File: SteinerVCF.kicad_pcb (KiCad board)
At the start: 2 copper layers, 39.6 x 100 mm, 72 parts, among them J1 AudioJack2_Ground_Switch, J2 AudioJack2_Ground_Switch, J3 AudioJack2_Ground_Switch, J4 AudioJack2_Ground_Switch, J5 AudioJack2_Ground_Switch, J6 AudioJack2_Ground_Switch, J7 Conn_02x05_Odd_Even, J8 AudioJack2_Ground_Switch, J9 AudioJack2_Ground_Switch, Q1 BC847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

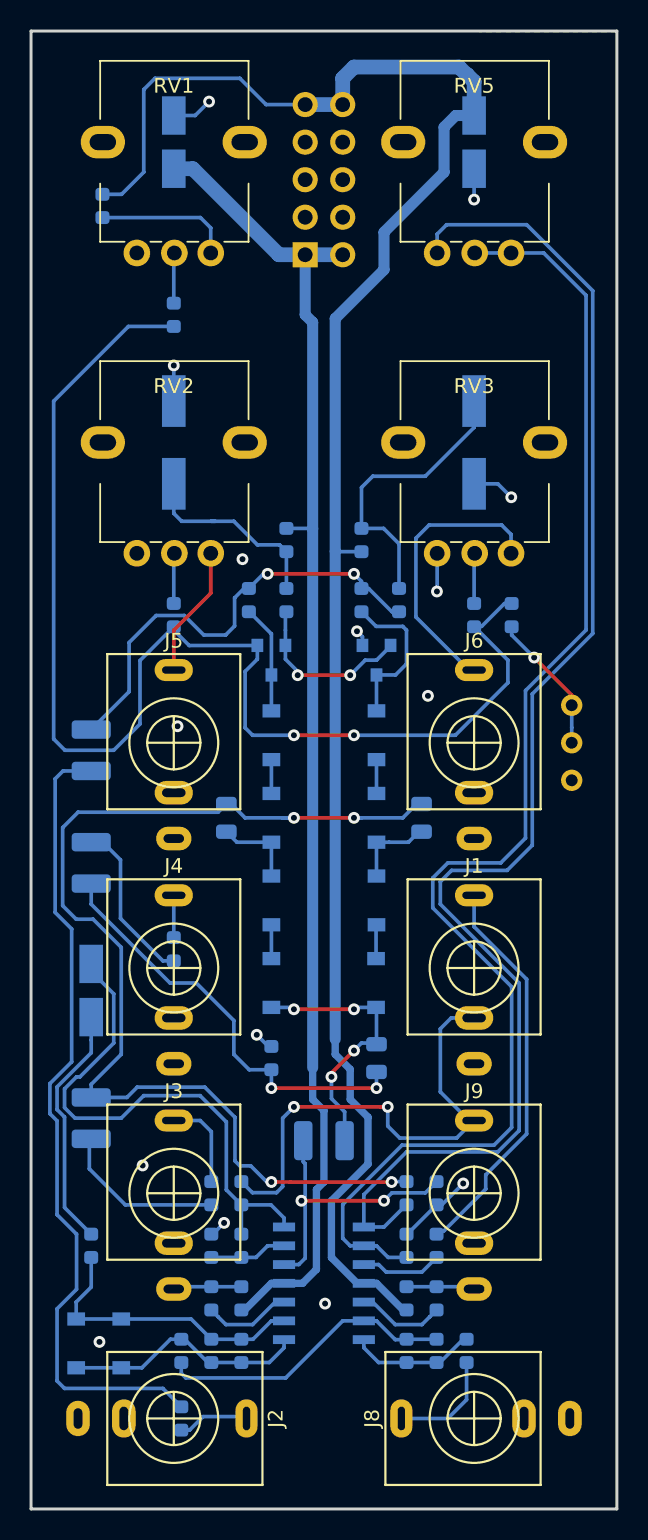
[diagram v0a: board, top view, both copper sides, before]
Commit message: Better placement of large caps.
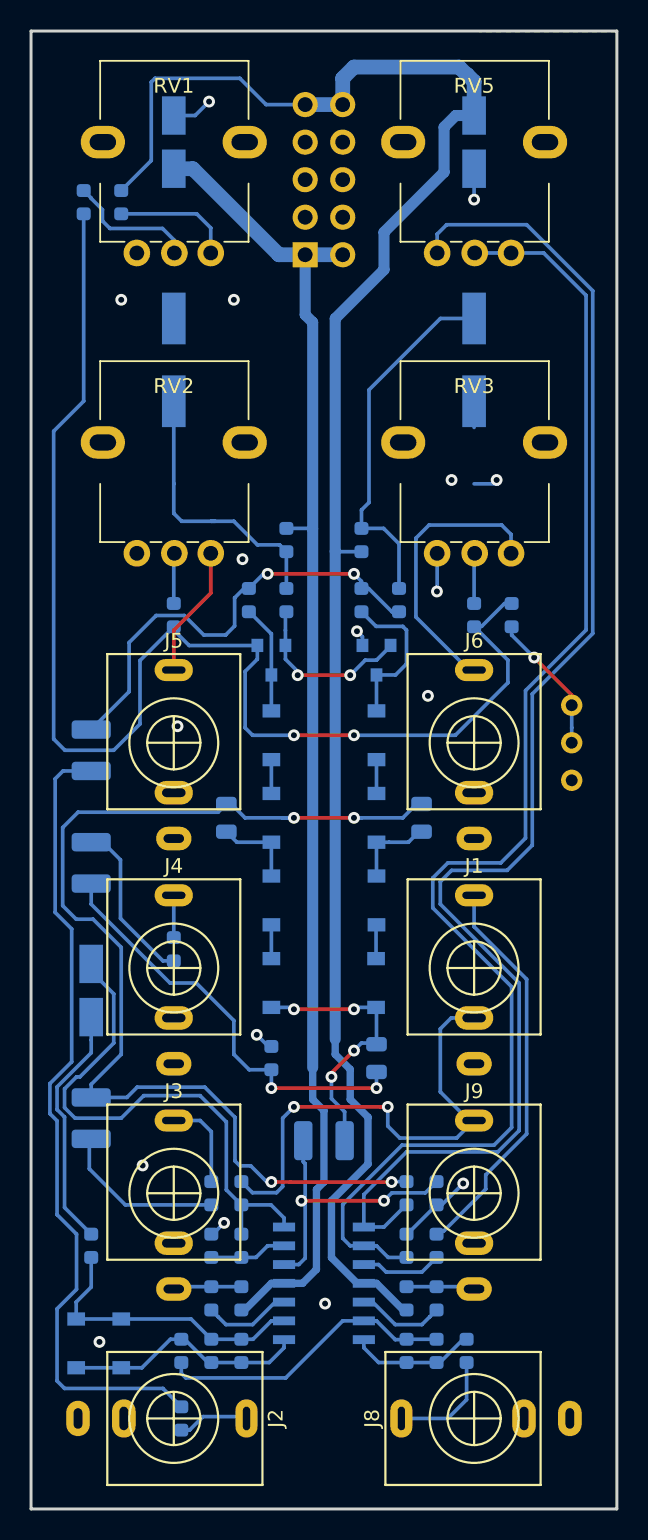
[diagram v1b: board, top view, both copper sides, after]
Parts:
- moved R4 9.76 mm to (132.2, 68.4)
- moved C6 5.59 mm to (138.3, 79.1)
- moved C7 5.59 mm to (158.7, 79.1)
- moved R1 1.30 mm to (134.8, 68.4)
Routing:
- net Net-(C6-Pad2): track 13.5 -> 19.1 mm
- net /CutOff: track 3.41 -> 8.90 mm
- net Net-(C7-Pad1): track 19.8 -> 24.7 mm
- net Net-(Q1-Pad1): track 87.1 -> 90.4 mm
- net GND: track 30.9 -> 29.3 mm, vias 15 -> 17
- net +12V: track 129.4 -> 127.8 mm
- net Net-(R1-Pad1): track 9.37 -> 8.20 mm
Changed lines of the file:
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@@
     (thickness 1.6)
     (drawings 58)
-    (tracks 499)
+    (tracks 508)
     (zones 0)
     (modules 72)
@@
   )
   (module Capacitor_SMD:CP_Elec_6.3x5.4 (layer B.Cu)
-    (at 138.34 84.68 270)
+    (at 138.34 79.092 270)
     (descr "SMT capacitor, aluminium electrolytic, 6.3x5.4, Panasonic C55 ")
     (tags "Capacitor Electrolytic")
@@
   )
   (module Capacitor_SMD:CP_Elec_6.3x5.4 (layer B.Cu)
-    (at 158.66 84.68 270)
+    (at 158.66 79.092 270)
     (descr "SMT capacitor, aluminium electrolytic, 6.3x5.4, Panasonic C55 ")
     (tags "Capacitor Electrolytic")
@@
   )
   (module Resistor_SMD:R_0603_1608Metric (layer B.Cu)
-    (at 138.34 76.044 90)
+    (at 132.244 68.424 90)
     (descr "Resistor SMD 0603 (1608 Metric), square (rectangular) end terminal, IPC_7351 nominal, (Body size source: http://www.tortai-tech.com/upload/download/2011102023233369053.pdf), generated with kicad-footprint-generator")
     (tags resistor)
@@
   )
   (module Resistor_SMD:R_0603_1608Metric (layer B.Cu)
-    (at 133.514 68.678 90)
+    (at 134.784 68.424 90)
     (descr "Resistor SMD 0603 (1608 Metric), square (rectangular) end terminal, IPC_7351 nominal, (Body size source: http://www.tortai-tech.com/upload/download/2011102023233369053.pdf), generated with kicad-footprint-generator")
     (tags resistor)
@@
   (segment (start 150.75 141.576) (end 149.008 139.834) (width 0.5) (layer B.Cu) (net 20))
   (segment (start 151.2 141.576) (end 150.75 141.576) (width 0.5) (layer B.Cu) (net 20))
-  (segment (start 136.308 66.392) (end 134.8095 67.8905) (width 0.25) (layer B.Cu) (net 20))
-  (segment (start 136.308 60.804) (end 136.308 66.392) (width 0.25) (layer B.Cu) (net 20))
-  (segment (start 137.07 60.042) (end 136.308 60.804) (width 0.25) (layer B.Cu) (net 20))
-  (segment (start 134.8095 67.8905) (end 133.514 67.8905) (width 0.25) (layer B.Cu) (net 20))
-  (segment (start 144.5884 61.82) (end 142.8104 60.042) (width 0.25) (layer B.Cu) (net 20))
+  (segment (start 136.816 60.296) (end 136.816 65.6045) (width 0.25) (layer B.Cu) (net 20))
   (segment (start 142.8104 60.042) (end 137.07 60.042) (width 0.25) (layer B.Cu) (net 20))
+  (segment (start 136.816 65.6045) (end 134.784 67.6365) (width 0.25) (layer B.Cu) (net 20))
+  (segment (start 144.5884 61.82) (end 142.8104 60.042) (width 0.25) (layer B.Cu) (net 20))
+  (segment (start 137.07 60.042) (end 136.816 60.296) (width 0.25) (layer B.Cu) (net 20))
   (segment (start 147.23 61.82) (end 144.5884 61.82) (width 0.25) (layer B.Cu) (net 20))
   (segment (start 140.88 71.90001) (end 140.84 71.86001) (width 0.25) (layer B.Cu) (net 21))
-  (segment (start 140.84 70.162) (end 140.84 71.86001) (width 0.25) (layer B.Cu) (net 21))
-  (segment (start 140.1435 69.4655) (end 140.84 70.162) (width 0.25) (layer B.Cu) (net 21))
-  (segment (start 133.514 69.4655) (end 140.1435 69.4655) (width 0.25) (layer B.Cu) (net 21))
+  (segment (start 140.84 70.162) (end 139.8895 69.2115) (width 0.25) (layer B.Cu) (net 21))
+  (segment (start 139.8895 69.2115) (end 134.784 69.2115) (width 0.25) (layer B.Cu) (net 21))
+  (segment (start 140.84 71.86001) (end 140.84 70.162) (width 0.25) (layer B.Cu) (net 21))
   (segment (start 138.346 87.48) (end 138.34 87.48) (width 0.25) (layer B.Cu) (net 22))
   (segment (start 145.96 94.5605) (end 145.9345 94.5605) (width 0.25) (layer B.Cu) (net 22))
@@
   (segment (start 153.58 91.538) (end 152.5385 90.4965) (width 0.25) (layer B.Cu) (net 26))
   (segment (start 153.58 94.5605) (end 153.58 91.538) (width 0.25) (layer B.Cu) (net 26))
-  (segment (start 151.04 87.728) (end 151.04 90.4965) (width 0.25) (layer B.Cu) (net 26))
-  (segment (start 151.802 86.966) (end 151.04 87.728) (width 0.25) (layer B.Cu) (net 26))
-  (segment (start 158.66 83.664) (end 155.358 86.966) (width 0.25) (layer B.Cu) (net 26))
-  (segment (start 155.358 86.966) (end 151.802 86.966) (width 0.25) (layer B.Cu) (net 26))
-  (segment (start 158.66 81.88) (end 158.66 83.664) (width 0.25) (layer B.Cu) (net 26))
+  (segment (start 156.38 76.292) (end 158.66 76.292) (width 0.25) (layer B.Cu) (net 26))
+  (segment (start 151.548 81.124) (end 156.38 76.292) (width 0.25) (layer B.Cu) (net 26))
+  (segment (start 151.548 88.744) (end 151.548 81.124) (width 0.25) (layer B.Cu) (net 26))
+  (segment (start 151.04 89.252) (end 151.548 88.744) (width 0.25) (layer B.Cu) (net 26))
+  (segment (start 151.04 90.4965) (end 151.04 89.252) (width 0.25) (layer B.Cu) (net 26))
+  (segment (start 158.66 81.88) (end 158.66 83.664) (width 0.25) (layer B.Cu) (net 55))
   (segment (start 165.264 103.981767) (end 165.264 102.46) (width 0.25) (layer B.Cu) (net 27))
   (segment (start 165.264 105) (end 165.264 103.981767) (width 0.25) (layer B.Cu) (net 27))
@@
   (segment (start 134.276 105.508) (end 136.054 103.73) (width 0.25) (layer B.Cu) (net 28))
   (segment (start 130.212 104.746) (end 130.974 105.508) (width 0.25) (layer B.Cu) (net 28))
-  (segment (start 130.212 81.886) (end 130.212 104.746) (width 0.25) (layer B.Cu) (net 28))
-  (segment (start 135.2665 76.8315) (end 130.212 81.886) (width 0.25) (layer B.Cu) (net 28))
   (segment (start 130.974 105.508) (end 134.276 105.508) (width 0.25) (layer B.Cu) (net 28))
   (segment (start 136.054 99.4375) (end 138.34 97.1515) (width 0.25) (layer B.Cu) (net 28))
-  (segment (start 138.34 76.8315) (end 135.2665 76.8315) (width 0.25) (layer B.Cu) (net 28))
   (segment (start 139.3814 98.4214) (end 138.34 97.38) (width 0.25) (layer B.Cu) (net 28))
   (segment (start 138.34 97.38) (end 138.34 97.1515) (width 0.25) (layer B.Cu) (net 28))
   (segment (start 143.9846 98.4214) (end 139.3814 98.4214) (width 0.25) (layer B.Cu) (net 28))
   (segment (start 143.994 98.412) (end 143.9846 98.4214) (width 0.25) (layer B.Cu) (net 28))
+  (segment (start 132.244 81.886) (end 130.212 83.918) (width 0.25) (layer B.Cu) (net 28))
+  (segment (start 130.212 83.918) (end 130.212 104.746) (width 0.25) (layer B.Cu) (net 28))
+  (segment (start 132.244 69.2115) (end 132.244 81.886) (width 0.25) (layer B.Cu) (net 28))
   (segment (start 144.944 102.842) (end 144.944 100.412) (width 0.25) (layer B.Cu) (net 29))
   (segment (start 144.944 97.634) (end 143.4455 96.1355) (width 0.25) (layer B.Cu) (net 29))
@@
   (segment (start 130.844 106.908) (end 130.3136 107.4384) (width 0.25) (layer B.Cu) (net 35))
   (segment (start 138.34 71.90001) (end 138.38 71.86001) (width 0.25) (layer B.Cu) (net 36))
-  (segment (start 138.34 75.2565) (end 138.34 71.90001) (width 0.25) (layer B.Cu) (net 36))
+  (segment (start 132.752 68.1445) (end 132.244 67.6365) (width 0.25) (layer B.Cu) (net 36))
+  (segment (start 133.514 68.932) (end 132.752 68.17) (width 0.25) (layer B.Cu) (net 36))
+  (segment (start 133.514 69.694) (end 133.514 68.932) (width 0.25) (layer B.Cu) (net 36))
+  (segment (start 132.752 68.17) (end 132.752 68.1445) (width 0.25) (layer B.Cu) (net 36))
+  (segment (start 138.38 71.86001) (end 138.38 71.004) (width 0.25) (layer B.Cu) (net 36))
+  (segment (start 134.022 70.202) (end 133.514 69.694) (width 0.25) (layer B.Cu) (net 36))
+  (segment (start 137.578 70.202) (end 134.022 70.202) (width 0.25) (layer B.Cu) (net 36))
+  (segment (start 138.38 71.004) (end 137.578 70.202) (width 0.25) (layer B.Cu) (net 36))
   (segment (start 158.66 92.22001) (end 158.7 92.18001) (width 0.25) (layer B.Cu) (net 37))
   (segment (start 158.66 95.5765) (end 158.66 92.22001) (width 0.25) (layer B.Cu) (net 37))
@@
   (segment (start 141.896 111.0175) (end 142.6085 111.73) (width 0.25) (layer B.Cu) (net 53))
   (segment (start 144.944 108.43) (end 144.944 106.142) (width 0.25) (layer B.Cu) (net 54))
-  (via (at 138.34 79.473) (size 0.8) (drill 0.4) (layers F.Cu B.Cu) (net 55))
-  (segment (start 138.34 81.88) (end 138.34 79.473) (width 0.25) (layer B.Cu) (net 55))
+  (segment (start 138.34 87.48) (end 138.34 81.892) (width 0.25) (layer B.Cu) (net 22))
   (via (at 158.66 68.2462) (size 0.8) (drill 0.4) (layers F.Cu B.Cu) (net 55))
   (segment (start 158.66 66.16) (end 158.66 68.2462) (width 0.25) (layer B.Cu) (net 55))
@@
   (segment (start 139.7844 62.56) (end 140.7276 61.6168) (width 0.25) (layer B.Cu) (net 55))
   (segment (start 138.34 62.56) (end 139.7844 62.56) (width 0.25) (layer B.Cu) (net 55))
-  (via (at 161.1746 88.3884) (size 0.8) (drill 0.4) (layers F.Cu B.Cu) (net 55))
-  (segment (start 160.2662 87.48) (end 161.1746 88.3884) (width 0.25) (layer B.Cu) (net 55))
-  (segment (start 158.66 87.48) (end 160.2662 87.48) (width 0.25) (layer B.Cu) (net 55))
   (via (at 156.1454 94.7638) (size 0.8) (drill 0.4) (layers F.Cu B.Cu) (net 55))
   (segment (start 156.16 94.7492) (end 156.1454 94.7638) (width 0.25) (layer B.Cu) (net 55))
@@
   (segment (start 140.88 138.2485) (end 140.9817 138.2485) (width 0.25) (layer B.Cu) (net 55))
   (via (at 142.9882 92.5794) (size 0.8) (drill 0.4) (layers F.Cu B.Cu) (net 55))
+  (segment (start 160.2662 87.48) (end 158.66 87.48) (width 0.25) (layer B.Cu) (net 55))
+  (segment (start 160.184 87.22) (end 160.2662 87.48) (width 0.25) (layer B.Cu) (net 55))
+  (via (at 160.184 87.22) (size 0.8) (drill 0.4) (layers F.Cu B.Cu) (net 55))
+  (via (at 157.136 87.22) (size 0.8) (drill 0.4) (layers F.Cu B.Cu) (net 55))
+  (via (at 142.404 75.028) (size 0.8) (drill 0.4) (layers F.Cu B.Cu) (net 55))
+  (via (at 134.784 75.028) (size 0.8) (drill 0.4) (layers F.Cu B.Cu) (net 55))
   (zone (net 55) (net_name GND) (layer F.Cu) (hatch edge 0.508)
     (connect_pads (clearance 0.508))

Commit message: Moved some caps away from the edge.
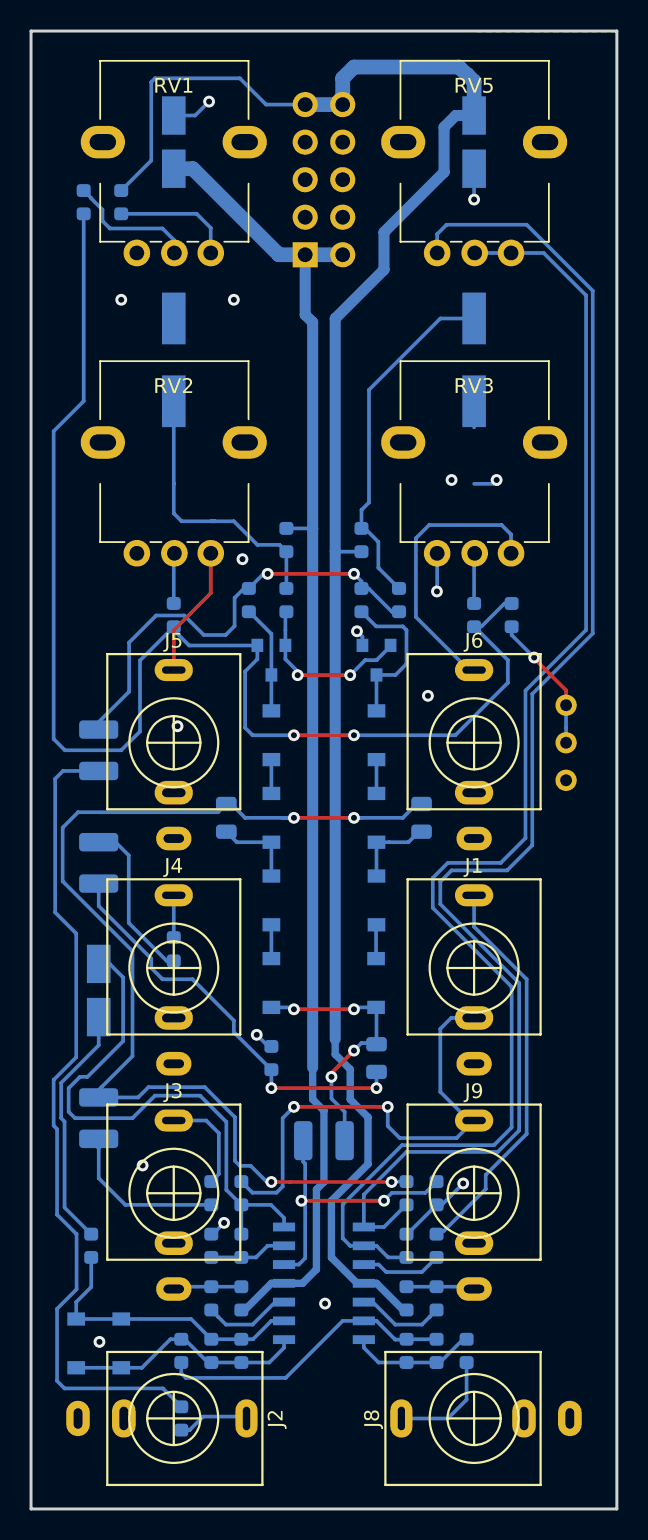
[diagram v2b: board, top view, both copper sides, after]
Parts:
- moved C1 0.51 mm to (133.3, 105.5)
- moved C12 0.51 mm to (133.3, 121.8)
- moved C2 0.51 mm to (133.3, 130.4)
- moved C3 0.51 mm to (133.3, 113.1)
- moved RV4 0.38 mm to (164.9, 102.5)
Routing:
- net Net-(C12-Pad1): track 36.4 -> 37.6 mm
- net Net-(C7-Pad1): track 24.7 -> 23.9 mm
- net Net-(C3-Pad1): track 29.1 -> 28.3 mm
- net /BP: track 6.23 -> 6.89 mm
- net Net-(C1-Pad2): track 54.9 -> 55.5 mm
